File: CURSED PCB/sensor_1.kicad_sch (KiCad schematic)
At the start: 23 parts, among them J1 Conn_01x05_Socket, J2 Micro_SD_Card, Q1 PZTA42, U10 MCP2562, U12 AD5761BRUZ, U9 PIC18F26K83, Y1 27 MHzCrystal

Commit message: changes to something
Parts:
- JP1, JP2, JP3: footprint (none) -> Jumper:SolderJumper-2_P1.3mm_Bridged2Bar_Pad1.0x1.5mm
- U10: footprint (none) -> Package_SO:SOIC-8_3.9x4.9mm_P1.27mm
- U9: footprint (none) -> Package_SO:SOIC-28W_7.5x18.7mm_P1.27mm
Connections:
- net IRQ is gone; now on net IRQ/MDAT: U9.3 (RA1)
- net MKLVN is gone; now on net MKLKIN: U9.25 (RB4)
- net RXD/CANRX is gone; now on net RXD: U9.17 (RC6)
- net TXD/CANTX is gone; now on net TXD: U9.18 (RC7)
- net +3.3VA: no longer U12.4 (VREFIN), U12.8 (VDD)
- net CS: no longer J2.2 (DAT3/CD), U12.13 (~{SYNC})
- net at U9.16 (RC5): now also U12.13 (~{SYNC})
- net CS2: now reaches U9.2 (RA0)
- net CS2: now also J2.2 (DAT3/CD)
- new net V_AMP_OUT: U12.4 (VREFIN), U12.8 (VDD)
- no-connect marks 6 -> 16
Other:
- added sheet Booster Converthing Thing thing (boost.kicad_sch)
- note removed: "page done"
- moved on the sheet: Q1

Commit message: something related to current and stuff
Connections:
- net +3.3VA: now also U12.4 (VREFIN)
- net V_AMP_OUT: no longer U12.4 (VREFIN)
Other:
- note added: "24V"

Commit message: forgot to rename things
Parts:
- J1: value Conn_01x05_Socket -> Programming Header
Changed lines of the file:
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@@
 	(wire
 		(pts
-			(xy 74.93 40.64) (xy 81.28 40.64)
+			(xy 68.58 40.64) (xy 81.28 40.64)
 		)
 		(stroke
@@
 	(wire
 		(pts
-			(xy 83.82 45.72) (xy 87.63 45.72)
+			(xy 68.58 45.72) (xy 87.63 45.72)
 		)
 		(stroke
@@
 	)
 	(label "MCLR"
-		(at 74.93 40.64 180)
+		(at 68.58 40.64 180)
 		(effects
 			(font
@@
 	)
 	(label "IRQ{slash}MDAT"
-		(at 83.82 45.72 180)
+		(at 68.58 45.72 180)
 		(effects
 			(font
@@
 			)
 		)
-		(property "Value" "Conn_01x05_Socket"
+		(property "Value" "Programming Header"
 			(at 38.862 106.68 0)
 			(effects

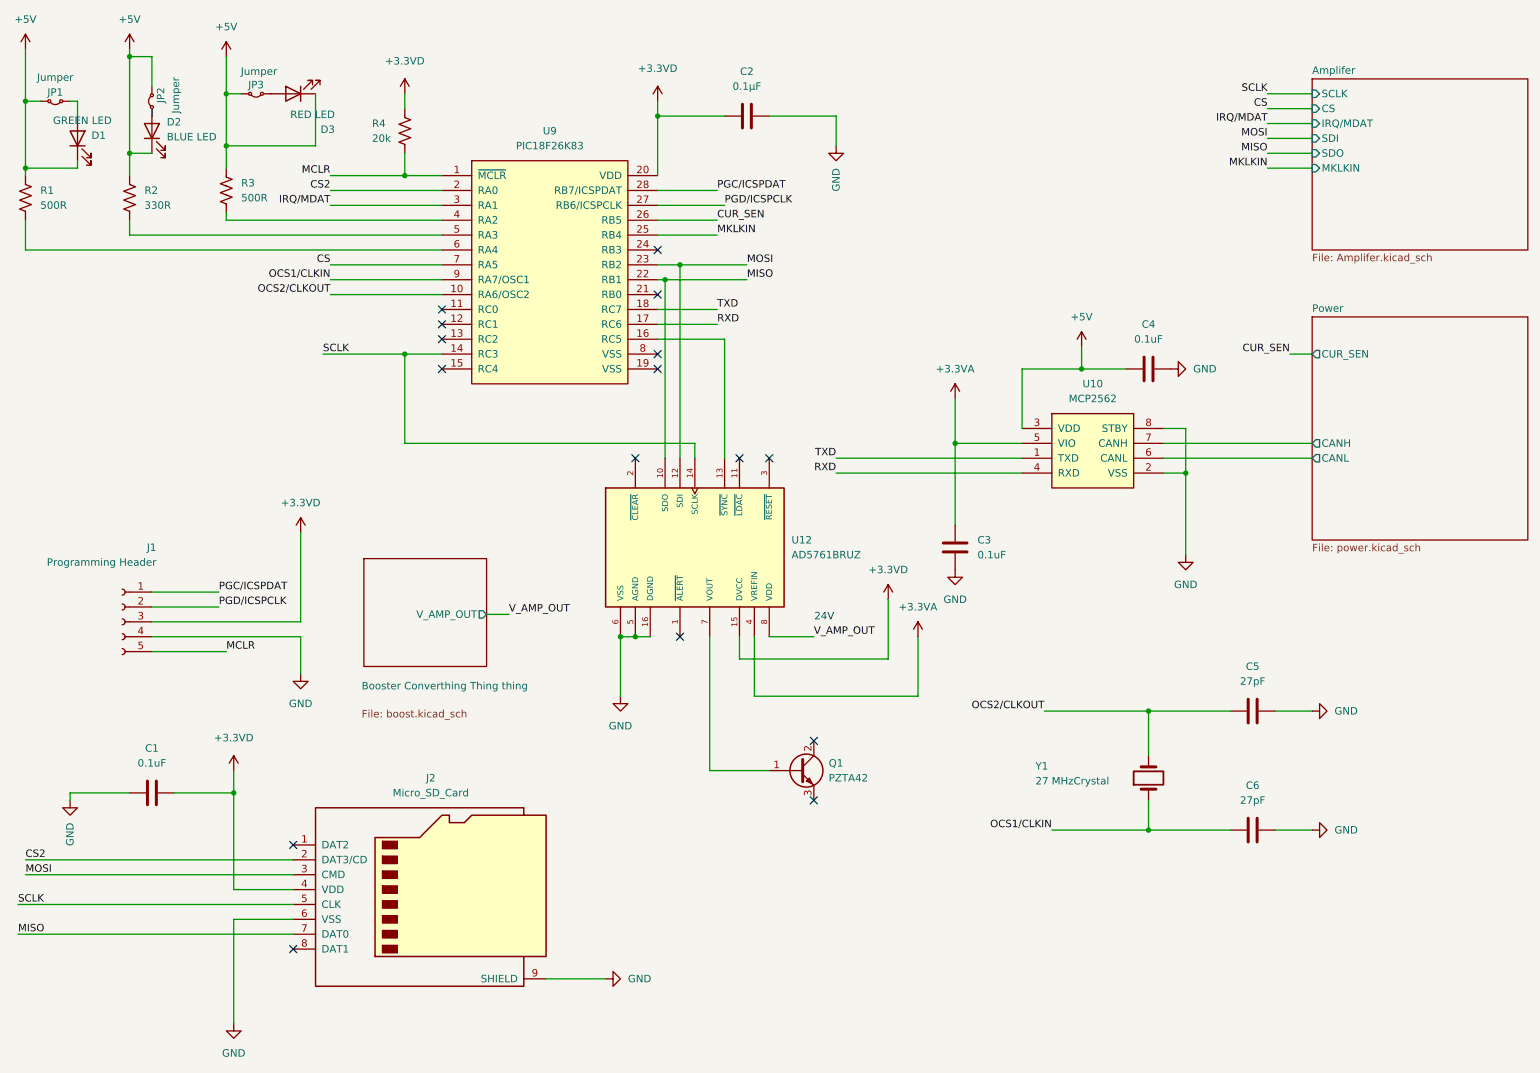
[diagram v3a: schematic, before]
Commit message: some fixes to conner critique
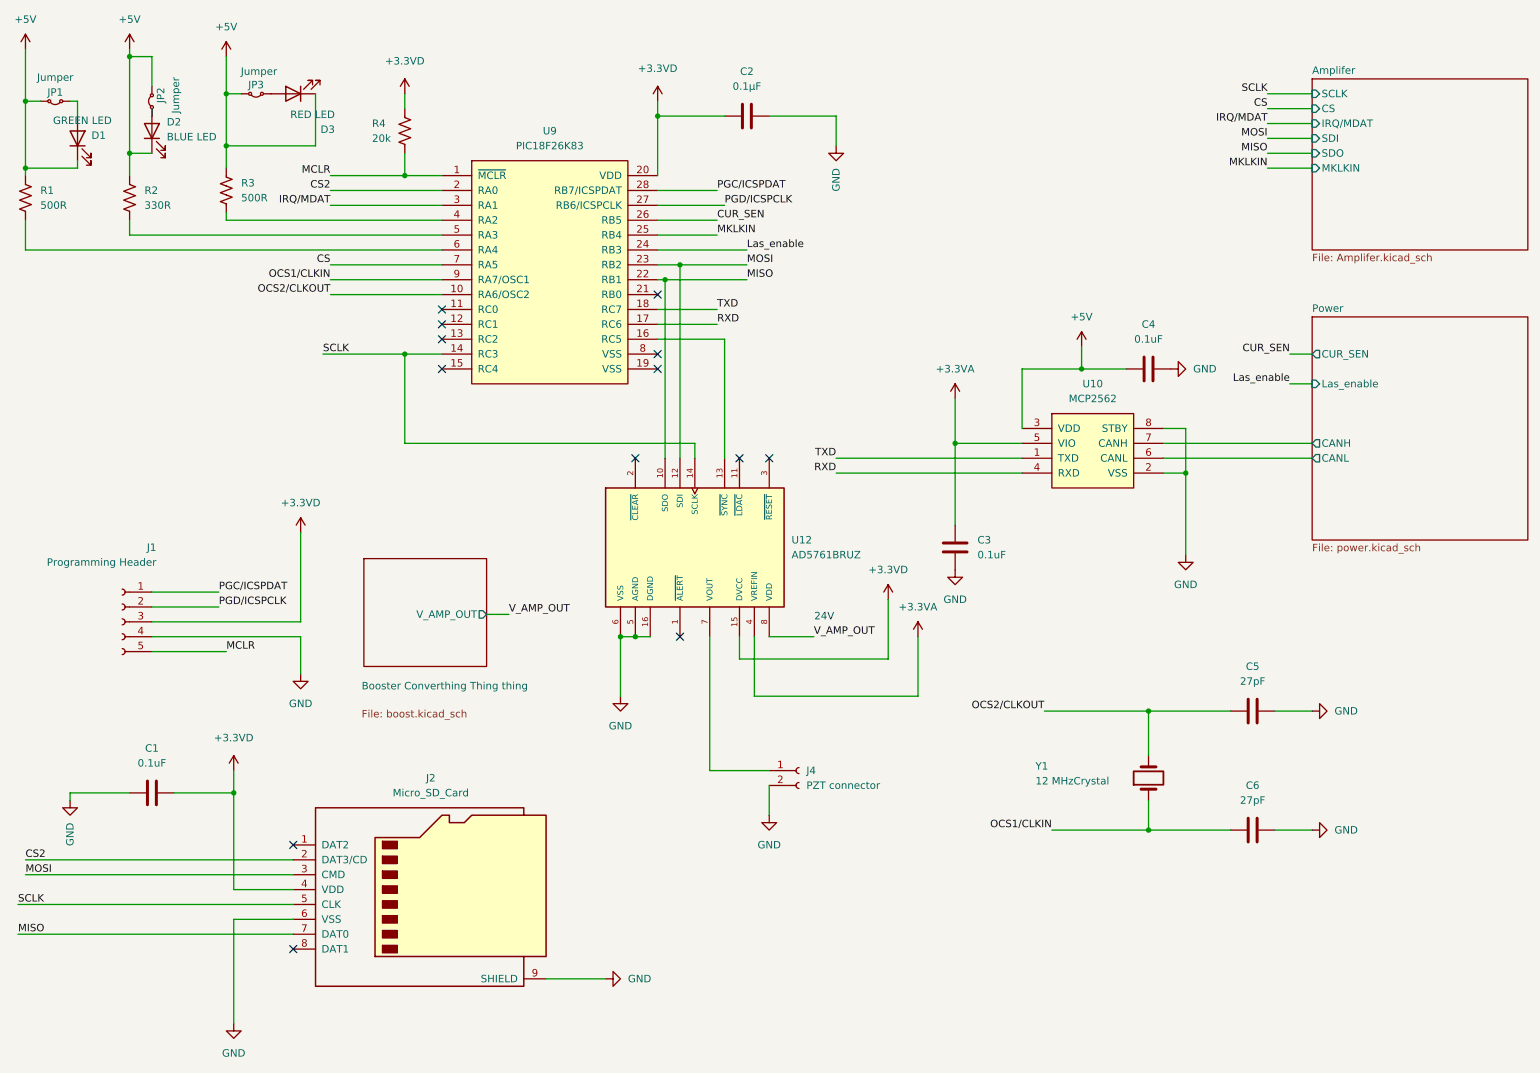
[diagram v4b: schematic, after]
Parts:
- removed Q1: PZTA42, Package_TO_SOT_SMD:SOT-223-3_TabPin2, symbol Transistor_BJT:PZTA42
- added J4: PZT connector, symbol Connector:Conn_01x02_Socket
- Y1: value 27 MHzCrystal -> 12 MHzCrystal
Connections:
- net GND: now also J4.2 (Pin_2)
- net Las_enable: now reaches U9.24 (RB3)
- net at U12.7 (VOUT): now also J4.1 (Pin_1)
- no-connect marks 16 -> 13
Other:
- sheet Power ports: added Las_enable; removed none
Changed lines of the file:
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@@
 	)
 	(no_connect
-		(at 151.13 147.32)
-	)
-	(no_connect
-		(at 124.46 53.34)
-	)
-	(no_connect
 		(at 62.23 154.94)
 	)
-	(no_connect
-		(at 151.13 137.16)
-	)
 	(wire
 		(pts
@@
 	(wire
 		(pts
+			(xy 143.51 144.78) (xy 143.51 149.86)
+		)
+		(stroke
+			(width 0)
+			(type default)
+		)
+	)
+	(wire
+		(pts
 			(xy 25.4 27.94) (xy 24.13 27.94)
 		)
@@
 	(wire
 		(pts
+			(xy 124.46 53.34) (xy 139.7 53.34)
+		)
+		(stroke
+			(width 0)
+			(type default)
+		)
+	)
+	(wire
+		(pts
 			(xy 208.28 132.08) (xy 222.25 132.08)
 		)
@@
 	(wire
 		(pts
+			(xy 232.41 76.2) (xy 236.22 76.2)
+		)
+		(stroke
+			(width 0)
+			(type default)
+		)
+	)
+	(wire
+		(pts
 			(xy 95.25 115.57) (xy 99.06 115.57)
 		)
@@
 		)
 	)
+	(label "Las_enable"
+		(at 232.41 76.2 180)
+		(effects
+			(font
+				(size 1.27 1.27)
+			)
+			(justify right bottom)
+		)
+	)
 	(label "MOSI"
 		(at 139.7 55.88 0)
@@
 		)
 	)
+	(label "Las_enable"
+		(at 139.7 53.34 0)
+		(effects
+			(font
+				(size 1.27 1.27)
+			)
+			(justify left bottom)
+		)
+	)
 	(label "CS2"
 		(at 16.51 157.48 0)
@@
 			)
 		)
-		(property "Value" "27 MHzCrystal"
+		(property "Value" "12 MHzCrystal"
 			(at 188.976 144.018 90)
 			(effects
@@
 	(symbol
 		(lib_id "power:GND")
+		(at 143.51 149.86 0)
+		(unit 1)
+		(exclude_from_sim no)
+		(in_bom yes)
+		(on_board yes)
+		(dnp no)
+		(fields_autoplaced yes)
+		(property "Reference" "#PWR052"
+			(at 143.51 156.21 0)
+			(effects
+				(font
+					(size 1.27 1.27)
+				)
+				(hide yes)
+			)
+		)
+		(property "Value" "GND"
+			(at 143.51 154.94 0)
+			(effects
+				(font
+					(size 1.27 1.27)
+				)
+			)
+		)
+		(property "Footprint" ""
+			(at 143.51 149.86 0)
+			(effects
+				(font
+					(size 1.27 1.27)
+				)
+				(hide yes)
+			)
+		)
+		(property "Datasheet" ""
+			(at 143.51 149.86 0)
+			(effects
+				(font
+					(size 1.27 1.27)
+				)
+				(hide yes)
+			)
+		)
+		(property "Description" "Power symbol creates a global label with name \"GND\" , ground"
+			(at 143.51 149.86 0)
+			(effects
+				(font
+					(size 1.27 1.27)
+				)
+				(hide yes)
+			)
+		)
+		(pin "1"
+		)
+		(instances
+			(project ""
+				(path "/9fb1a86f-679c-4b88-9ed1-932f4f414580"
+					(reference "#PWR052")
+					(unit 1)
+				)
+			)
+		)
+	)
+	(symbol
+		(lib_id "power:GND")
 		(at 236.22 152.4 90)
 		(unit 1)
@@
 	)
 	(symbol
+		(lib_id "Connector:Conn_01x02_Socket")
+		(at 148.59 142.24 0)
+		(unit 1)
+		(exclude_from_sim no)
+		(in_bom yes)
+		(on_board yes)
+		(dnp no)
+		(fields_autoplaced yes)
+		(property "Reference" "J4"
+			(at 149.86 142.2399 0)
+			(effects
+				(font
+					(size 1.27 1.27)
+				)
+				(justify left)
+			)
+		)
+		(property "Value" "PZT connector"
+			(at 149.86 144.7799 0)
+			(effects
+				(font
+					(size 1.27 1.27)
+				)
+				(justify left)
+			)
+		)
+		(property "Footprint" ""
+			(at 148.59 142.24 0)
+			(effects
+				(font
+					(size 1.27 1.27)
+				)
+				(hide yes)
+			)
+		)
+		(property "Datasheet" "~"
+			(at 148.59 142.24 0)
+			(effects
+				(font
+					(size 1.27 1.27)
+				)
+				(hide yes)
+			)
+		)
+		(property "Description" "Generic connector, single row, 01x02, script generated"
+			(at 148.59 142.24 0)
+			(effects
+				(font
+					(size 1.27 1.27)
+				)
+				(hide yes)
+			)
+		)
+		(pin "2"
+		)
+		(pin "1"
+		)
+		(instances
+			(project ""
+				(path "/9fb1a86f-679c-4b88-9ed1-932f4f414580"
+					(reference "J4")
+					(unit 1)
+				)
+			)
+		)
+	)
+	(symbol
 		(lib_id "power:GND")
 		(at 212.09 73.66 90)
@@
 	)
 	(symbol
-		(lib_id "Transistor_BJT:PZTA42")
-		(at 148.59 142.24 0)
-		(unit 1)
-		(exclude_from_sim no)
-		(in_bom yes)
-		(on_board yes)
-		(dnp no)
-		(fields_autoplaced yes)
-		(property "Reference" "Q1"
-			(at 153.67 140.9699 0)
-			(effects
-				(font
-					(size 1.27 1.27)
-				)
-				(justify left)
-			)
-		)
-		(property "Value" "PZTA42"
-			(at 153.67 143.5099 0)
-			(effects
-				(font
-					(size 1.27 1.27)
-				)
-				(justify left)
-			)
-		)
-		(property "Footprint" "Package_TO_SOT_SMD:SOT-223-3_TabPin2"
-			(at 153.67 144.145 0)
-			(effects
-				(font
-					(size 1.27 1.27)
-					(italic yes)
-				)
-				(justify left)
-				(hide yes)
-			)
-		)
-		(property "Datasheet" "https://www.onsemi.com/pub/Collateral/PZTA42T1-D.PDF"
-			(at 148.59 142.24 0)
-			(effects
-				(font
-					(size 1.27 1.27)
-				)
-				(justify left)
-				(hide yes)
-			)
-		)
-		(property "Description" "0.5A Ic, 300V Vce, NPN High Voltage Transistor, SOT-223"
-			(at 148.59 142.24 0)
-			(effects
-				(font
-					(size 1.27 1.27)
-				)
-				(hide yes)
-			)
-		)
-		(pin "3"
-		)
-		(pin "1"
-		)
-		(pin "2"
-		)
-		(instances
-			(project ""
-				(path "/9fb1a86f-679c-4b88-9ed1-932f4f414580"
-					(reference "Q1")
-					(unit 1)
-				)
-			)
-		)
-	)
-	(symbol
 		(lib_id "power:+3.3VA")
 		(at 63.5 101.6 0)
@@
 			(effects
 				(font
+					(size 1.27 1.27)
+				)
+				(justify left)
+			)
+		)
+		(pin "Las_enable" input
+			(at 236.22 76.2 180)
+			(effects
+				(font

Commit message: Small changes
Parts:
- removed J4: PZT connector, symbol Connector:Conn_01x02_Socket
- removed U9: PIC18F26K83, Package_SO:SOIC-28W_7.5x18.7mm_P1.27mm, symbol canhw:PIC18F26K83
- removed Y1: 12 MHzCrystal, Crystal:Crystal_HC49-4H_Vertical, symbol Device:Crystal
- added J4: 2 Wire Block for PZT, 691137710002:691137710002, symbol 691137710002:691137710002
- added TP1: SCLK TP, TestPoint:TestPoint_Loop_D2.50mm_Drill1.0mm, symbol Connector:TestPoint
- added TP4: MOSI TP, TestPoint:TestPoint_Loop_D2.50mm_Drill1.0mm, symbol Connector:TestPoint
- added TP5: MISO TP, TestPoint:TestPoint_Loop_D2.50mm_Drill1.0mm, symbol Connector:TestPoint
- added U3: STM32G431KBT6, STM32G431KBT6:QFP80P900X900X160-32N, symbol STM32G431KBT6:STM32G431KBT6
- added Y1: Crystal_GND24, Crystal:Crystal_SMD_Abracon_ABM8G-4Pin_3.2x2.5mm, symbol Device:Crystal_GND24
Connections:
- net +3.3VD: no longer C2.1
- net +5V: now also D3.2 (A), JP3.1 (A)
- net CS: now also U3.9 (PA4)
- net CS2: now also U3.25 (PA15)
- net GND: now also J4.2, U3.14 (VSSA), U3.16 (VSS), U3.32 (VSS)
- net MISO: now also U12.12 (SDI), TP5.1, U3.11 (PA6); no longer U12.10 (SDO)
- net MOSI: now also U12.10 (SDO), TP4.1, U3.12 (PA7); no longer U12.12 (SDI)
- net OCS1/CLKIN: now also U3.2 (PF0-OSC_IN), Y1.3
- net OCS2/CLKOUT: now also U3.3 (PF1-OSC_OUT), Y1.1
- net SCLK: now also TP1.1, U3.10 (PA5)
- net at U12.7 (VOUT): now also J4.1
- net CS_DAC: now reaches U12.13 (~{SYNC})
- net CS_DAC: now also U3.13 (PB0)
- new net VDD: C2.1, U3.1 (VDD), U3.17 (VDD)
- no-connect marks 13 -> 5
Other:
- moved on the sheet: C2, D3, JP3, R3, R4, U12

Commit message: file
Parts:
- removed D1: GREEN LED, LED_SMD:LED_0201_0603Metric, symbol Device:LED
- removed D3: RED LED, LED_SMD:LED_0201_0603Metric, symbol Device:LED
- removed JP1, JP3: Jumper, Jumper:SolderJumper-2_P1.3mm_Bridged2Bar_Pad1.0x1.5mm, symbol Jumper:Jumper_2_Small_Bridged
- removed R1, R3: 500R, Resistor_SMD:R_0201_0603Metric, symbol Device:R_US
- removed R4: 20k, Resistor_SMD:R_0201_0603Metric, symbol Device:R_US
- added C7: 0.1µF, Capacitor_SMD:C_0603_1608Metric_Pad1.08x0.95mm_HandSolder, symbol PCM_Capacitor_US_AKL:C_0201
- C1, C2, C3, C4, C5, C6: footprint Capacitor_SMD:C_0201_0603Metric_Pad0.64x0.40mm_HandSolder -> Capacitor_SMD:C_0603_1608Metric_Pad1.08x0.95mm_HandSolder
- D2: footprint LED_SMD:LED_0201_0603Metric -> LED_SMD:LED_0603_1608Metric_Pad1.05x0.95mm_HandSolder
- R2: footprint Resistor_SMD:R_0201_0603Metric -> Resistor_SMD:R_0603_1608Metric_Pad0.98x0.95mm_HandSolder
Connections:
- net VDD is gone; now on net +3.3VD: C2.1, U3.1 (VDD), U3.17 (VDD)
- net +3.3VA: now also U3.15 (VDDA/VREF+), C7.1
- net +3.3VD: now also D2.1 (K), JP2.2 (B), R2.1
- net +5V: no longer D2.1 (K), JP2.2 (B), R2.1
- net CUR_SEN: now also U3.29 (PB6)
- net GND: now also Y1.2, Y1.4, C7.2
- net IRQ/MDAT: now also U3.6 (PA1)
- net Las_enable: now also U3.30 (PB7)
- net MCLR: now also U3.4 (PG10-NRST)
- net PGC/ICSPDAT: now also U3.23 (PA13)
- net PGD/ICSPCLK: now also U3.24 (PA14)
- net RXD: now also U3.19 (PA9)
- net TXD: now also U3.18 (PA8)
- net at R2.2: now also U3.8 (PA3)
- no-connect marks 5 -> 16
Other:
- sheet Booster Converthing Thing thing renamed Booster
- moved on the sheet: C1, C2, R2

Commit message: more light
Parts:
- R2: value 330R -> 22R
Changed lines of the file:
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@@
 			)
 		)
-		(property "Value" "330R"
+		(property "Value" "22R"
 			(at 36.83 44.4499 0)
 			(effects

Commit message: connected stuff for pcb
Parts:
- Y1: value Crystal_GND24 -> 24Hz crystal
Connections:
- net RXD: now also U3.20 (PA10); no longer U3.19 (PA9)
- net TXD: now also U3.19 (PA9); no longer U3.18 (PA8)
- no-connect marks 16 -> 12
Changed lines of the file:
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@@
-	)
-	(no_connect
-		(at 85.09 66.04)
 	)
 	(no_connect
@@
 	)
 	(no_connect
-		(at 85.09 67.31)
-	)
-	(no_connect
 		(at 125.73 41.91)
 	)
@@
 	)
 	(no_connect
-		(at 85.09 69.85)
-	)
-	(no_connect
 		(at 125.73 44.45)
 	)
@@
 	)
 	(no_connect
-		(at 86.36 64.77)
-	)
-	(no_connect
 		(at 62.23 154.94)
 	)
@@
 	(wire
 		(pts
-			(xy 72.39 59.69) (xy 85.09 59.69)
+			(xy 72.39 62.23) (xy 85.09 62.23)
 		)
 		(stroke
@@
 	(wire
 		(pts
-			(xy 72.39 62.23) (xy 85.09 62.23)
+			(xy 72.39 64.77) (xy 85.09 64.77)
 		)
 		(stroke
@@
 	)
 	(label "MKLKIN"
-		(at 71.12 66.04 0)
+		(at 63.5 66.04 0)
 		(effects
 			(font
@@
 	)
 	(label "RXD"
-		(at 72.39 62.23 180)
+		(at 72.39 64.77 180)
 		(effects
 			(font
@@
 	)
 	(label "TXD"
-		(at 72.39 59.69 180)
+		(at 72.39 62.23 180)
 		(effects
 			(font
@@
 		(fields_autoplaced yes)
 		(property "Reference" "Y1"
-			(at 219.71 135.8198 90)
-			(effects
-				(font
-					(size 1.27 1.27)
-				)
-			)
-		)
-		(property "Value" "Crystal_GND24"
-			(at 219.71 138.3598 90)
-			(effects
-				(font
+			(at 218.44 135.8198 90)
+			(effects
+				(font
+					(size 1.27 1.27)
+				)
+			)
+		)
+		(property "Value" "24Hz crystal"
+			(at 218.44 138.3598 90)
+			(effects
+				(font
